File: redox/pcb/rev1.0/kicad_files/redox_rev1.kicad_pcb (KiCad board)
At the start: 2 copper layers, 162.2 x 126.5 mm, 86 parts, among them K0 KEYSW, K1 KEYSW, K10 KEYSW, K11 KEYSW, K12 KEYSW, K13 KEYSW, K14 KEYSW, K15 KEYSW, K16 KEYSW, K2 KEYSW, K20 KEYSW, K21 KEYSW, K22 KEYSW, K23 KEYSW, K24 KEYSW, K25 KEYSW, K26 KEYSW, K3 KEYSW, K30 KEYSW, K31 KEYSW, K32 KEYSW, K33 KEYSW, K34 KEYSW, K35 KEYSW, K36 KEYSW, K4 KEYSW, K40 KEYSW, K41 KEYSW, K42 KEYSW, K43 KEYSW, K44 KEYSW, K45 KEYSW, K46 KEYSW, K5 KEYSW, K6 KEYSW, U1 ProMicro

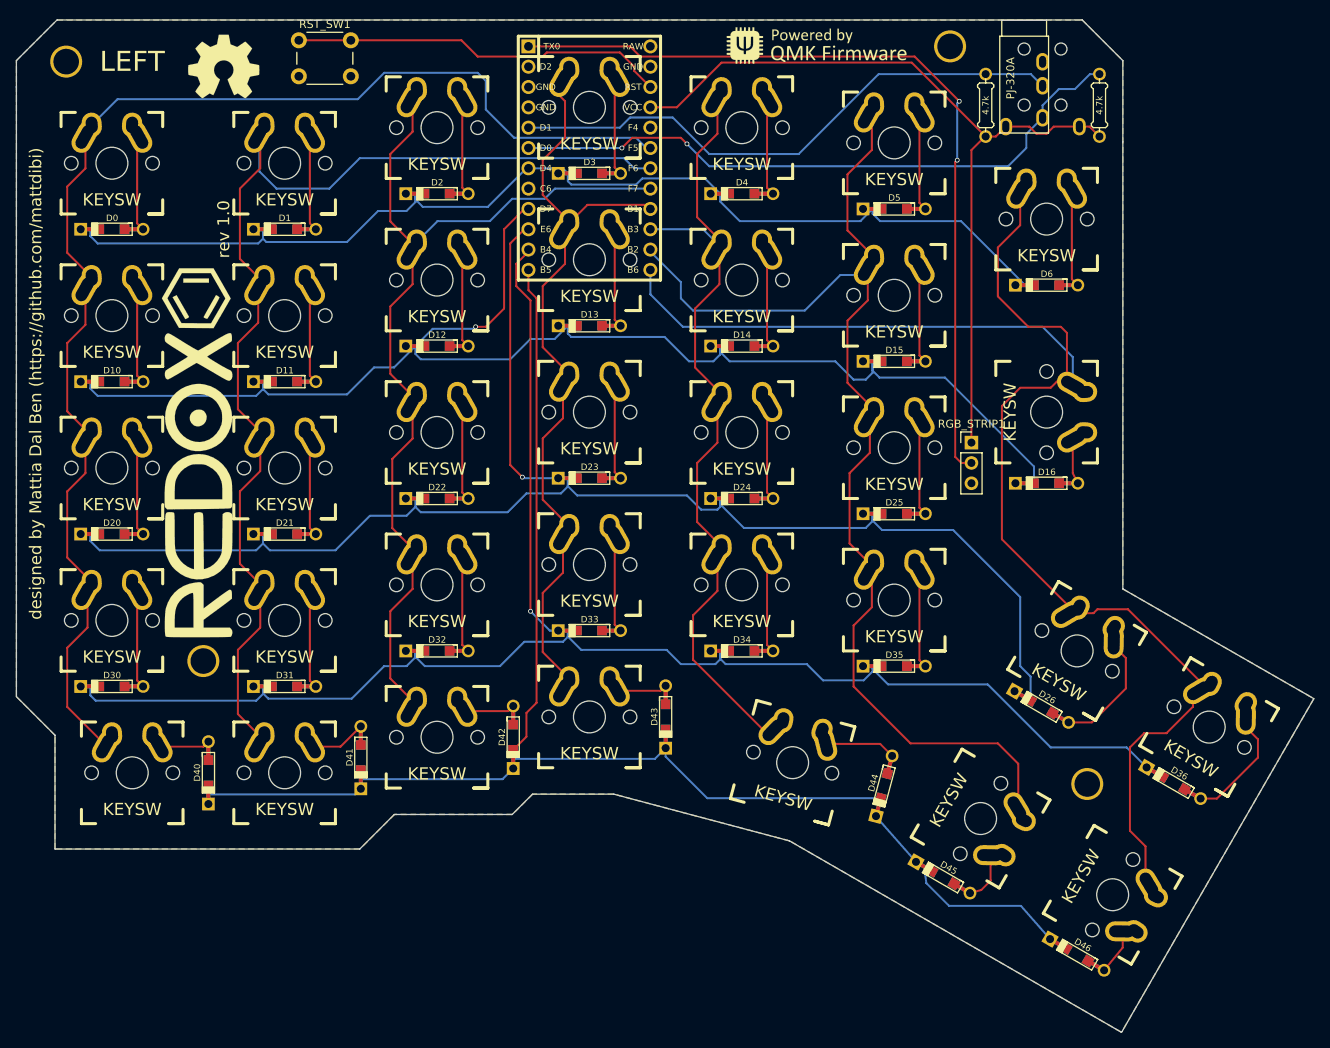
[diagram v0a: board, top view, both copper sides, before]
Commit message: change to kailh choc hotswap sockets
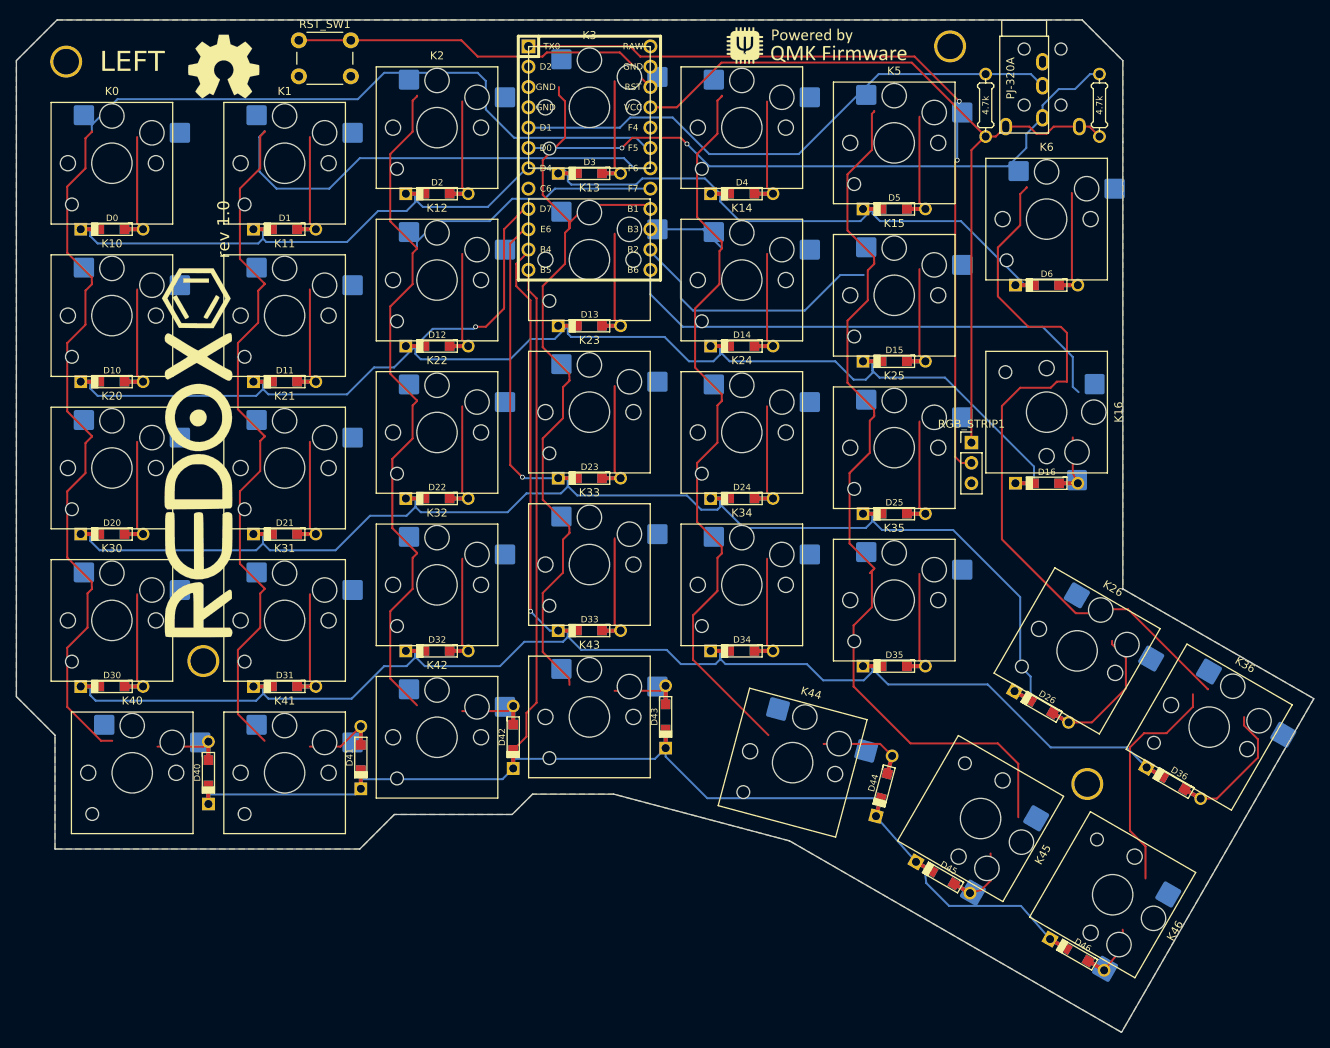
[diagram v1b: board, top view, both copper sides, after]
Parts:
- K0, K10, K20, K30, K44: footprint myparts:Mx_Alps_125-dualside -> PCM_Switch_Keyboard_Hotswap_Kailh:SW_Hotswap_Kailh_Choc_V1V2_1.25u
- K1, K11, K12, K13, K14, K15, K2, K21, K22, K23, K24, K25, K26, K3, K31, K32, K33, K34, K35, K36, K4, K40, K41, K42, K43, K5, K6: footprint canadian_footprints:Mx_Alps_100-dualside -> PCM_Switch_Keyboard_Hotswap_Kailh:SW_Hotswap_Kailh_Choc_V1V2_1.00u
- K16, K45, K46: footprint canadian_footprints:Mx_Alps_150-dualsided -> PCM_Switch_Keyboard_Hotswap_Kailh:SW_Hotswap_Kailh_Choc_V1V2_1.50u
- RGB_STRIP1: footprint Pin_Headers:Pin_Header_Straight_1x03_Pitch2.54mm -> redox_footprints:Pin_Header_Straight_1x03_Pitch2.54mm
- RST_SW1: footprint Buttons_Switches_ThroughHole:SW_PUSH_6mm_h4.3mm -> redox_footprints:SW_PUSH_6mm_h4.3mm
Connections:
- U1 pad 2: Net-(U1-Pad2) -> unconnected-(U1-RX1/PD2-Pad2)
- U1 pad 20: Net-(U1-Pad20) -> unconnected-(U1-A3/PF4-Pad20)
- U1 pad 24: Net-(U1-Pad24) -> unconnected-(U1-RAW-Pad24)
- U1 pad 8: Net-(U1-Pad8) -> unconnected-(U1-5/PC6-Pad8)
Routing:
- net Net-(D45-A): track 6.51 -> 0.00 mm
- net /Net-(D45-Pad2): track 0.00 -> 6.51 mm
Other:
- net class Default removed
- board text removed: "designed by Mattia Dal Ben (https://github.com/mattdibi)"
